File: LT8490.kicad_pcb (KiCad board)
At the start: 6 copper layers, 37.2 x 46 mm, 141 parts, among them J1 Conn_01x01, J10 Conn_01x01, J11 Conn_01x01, J12 Conn_01x01, J13 Conn_01x01, J14 Conn_01x01, J15 Conn_01x01, J16 Conn_01x01, J17 Conn_01x01, J18 Conn_01x01, J19 Conn_01x01, J2 Conn_01x01, J20 Conn_01x01, J21 Conn_01x01, J22 Conn_01x01, J23 Conn_01x01, J24 Conn_01x01, J25 Conn_01x01, J3 Conn_01x01, J4 Conn_01x01, J5 Conn_01x01, J6 Conn_01x01, J7 Conn_01x01, J8 Conn_01x01, J9 Conn_01x01, Q1 Si7106DN, Q2 Si7106DN, Q3 Si7106DN, Q4 Si7106DN, Q5 BSS84, Q6 MBT2222ADW1T1, U4 LT8490EUKJPBF

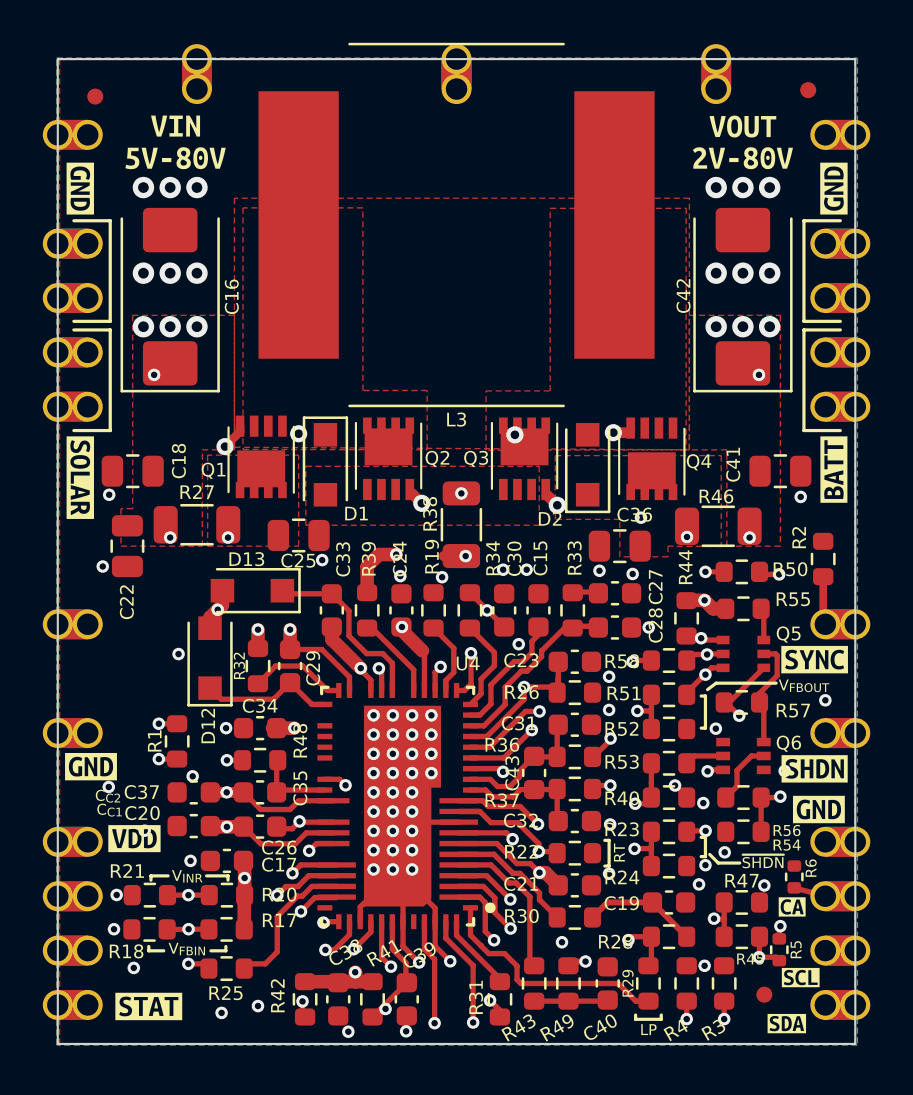
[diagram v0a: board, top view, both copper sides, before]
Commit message: changed some silkscreen
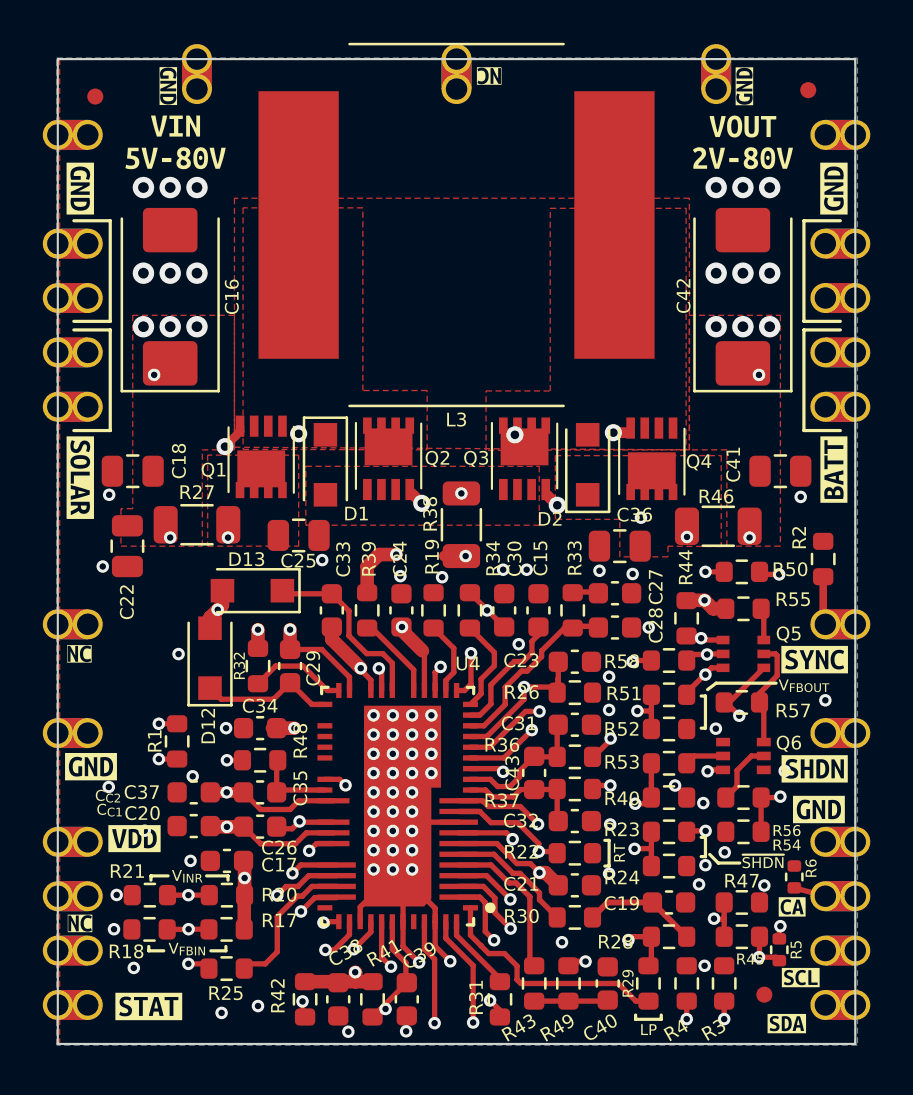
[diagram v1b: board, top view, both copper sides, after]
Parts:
- added kibuzzard-62D49DAC: G***, kibuzzard-62D49DAC, F.Cu at (130.3, 116.1)
- added kibuzzard-62D49DAC: G***, kibuzzard-62D49DAC, F.Cu at (130.3, 103.5)
- added kibuzzard-62D49DAC: G***, kibuzzard-62D49DAC, F.Cu at (149.4, 76.5)
- added kibuzzard-62D49DF0: G***, kibuzzard-62D49DF0, F.Cu at (161.3, 77.0)
- added kibuzzard-62D49DF0: G***, kibuzzard-62D49DF0, F.Cu at (134.4, 77.0)

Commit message: gerbers
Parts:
- moved Ref** 0.08 mm to (138.1, 121.1)
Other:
- board text added: "v00"

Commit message: tweaks after v00 build
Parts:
- R26: value 124K -> 23.7K
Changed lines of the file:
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@@
       (effects (font (size 0.635 0.635) (thickness 0.127)))
     )
-    (fp_text value "124K" (at 0 1.43) (layer "F.Fab")
+    (fp_text value "23.7K" (at 0 1.43) (layer "F.Fab")
       (effects (font (size 1 1) (thickness 0.15)))
     )
@@
     (connect_pads (clearance 0))
     (min_thickness 0.127)
-    (keepout (tracks allowed) (vias allowed) (pads allowed ) (copperpour not_allowed) (footprints allowed))
+    (keepout (tracks allowed) (vias allowed) (pads allowed) (copperpour not_allowed) (footprints allowed))
     (fill (thermal_gap 0.127) (thermal_bridge_width 0.508))
     (polygon
@@
     (connect_pads (clearance 0))
     (min_thickness 0.254)
-    (keepout (tracks allowed) (vias allowed) (pads allowed ) (copperpour not_allowed) (footprints allowed))
+    (keepout (tracks allowed) (vias allowed) (pads allowed) (copperpour not_allowed) (footprints allowed))
     (fill (thermal_gap 0.508) (thermal_bridge_width 0.508))
     (polygon

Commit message: minor tweaks after bench testing
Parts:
- added C1: 100nF, Capacitor_SMD:C_0603_1608Metric, F.Cu at (161.2, 113.7)
- added R7: 4, Resistor_SMD:R_0603_1608Metric, F.Cu at (134.6, 101.9)
- C20, C37: value 100nF -> 10nF
- R2: value 0 -> 10K
- R27: value 0.025 -> 0.1
- R44: value 0 -> 10
- R45: value 11.5K -> 18.2K
- moved D2 0.41 mm to (154.1, 95.1), turned to -90 degrees
- moved D1 0.40 mm to (141.8, 95.1)
- moved R47 0.10 mm to (161.2, 115.0)
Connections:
- D1 pad 2: Net-(D1-Pad2) -> GND
- D12 pad 2: GATEV_{CC} -> GATEV_{CC}`
- D13 pad 2: GATEV_{CC} -> GATEV_{CC}`
- D2 pad 1: V_{OUT} -> /V_{SW2}
- D2 pad 2: /V_{SW2} -> GND
- Q2 pad 1: Net-(D1-Pad2) -> /RS+
- Q2 pad 2: Net-(D1-Pad2) -> /RS+
- Q2 pad 3: Net-(D1-Pad2) -> /RS+
- Q3 pad 1: Net-(D1-Pad2) -> /RS+
- Q3 pad 2: Net-(D1-Pad2) -> /RS+
- Q3 pad 3: Net-(D1-Pad2) -> /RS+
- R36 pad 1: Net-(D1-Pad2) -> /RS+
- R38 pad 1: Net-(D1-Pad2) -> /RS+
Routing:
- net VBATT: track 41.5 -> 0.00 mm, vias 5 -> 3
- net /CSNOUT: track 0.00 -> 41.5 mm, vias 0 -> 2
- net Net-(D1-Pad2): track 17.2 -> 0.00 mm, vias 2 -> 0
- net /RS+: track 0.00 -> 17.2 mm, vias 0 -> 2
- net Net-(C25-Pad1): track 12.6 -> 0.00 mm, vias 1 -> 0
- net /CSNIN: track 0.00 -> 12.6 mm, vias 1 -> 2
- net GATEV_{CC}`: track 0.00 -> 3.94 mm
- net GATEV_{CC}: track 40.6 -> 42.2 mm
- net Net-(R45-Pad1): track 15.8 -> 17.2 mm
- net GND: vias 82 -> 72
- added copper zone on F.Cu, net /RS+
- removed copper zone on F.Cu, net Net-(D1-Pad2)
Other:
- board text added: "v01"
- board text removed: "v00"
- board text removed: "~{SHDN}"
